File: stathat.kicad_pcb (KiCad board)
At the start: 4 copper layers, 65 x 56.5 mm, 40 parts, among them J1 Raspberry_Pi_2_3, J27 Conn_01x01, J28 Conn_01x01, J29 Conn_01x01, J31 Conn_01x01, J32 Conn_01x01, U26 HCPL3700, U27 HCPL3700, U28 HCPL3700

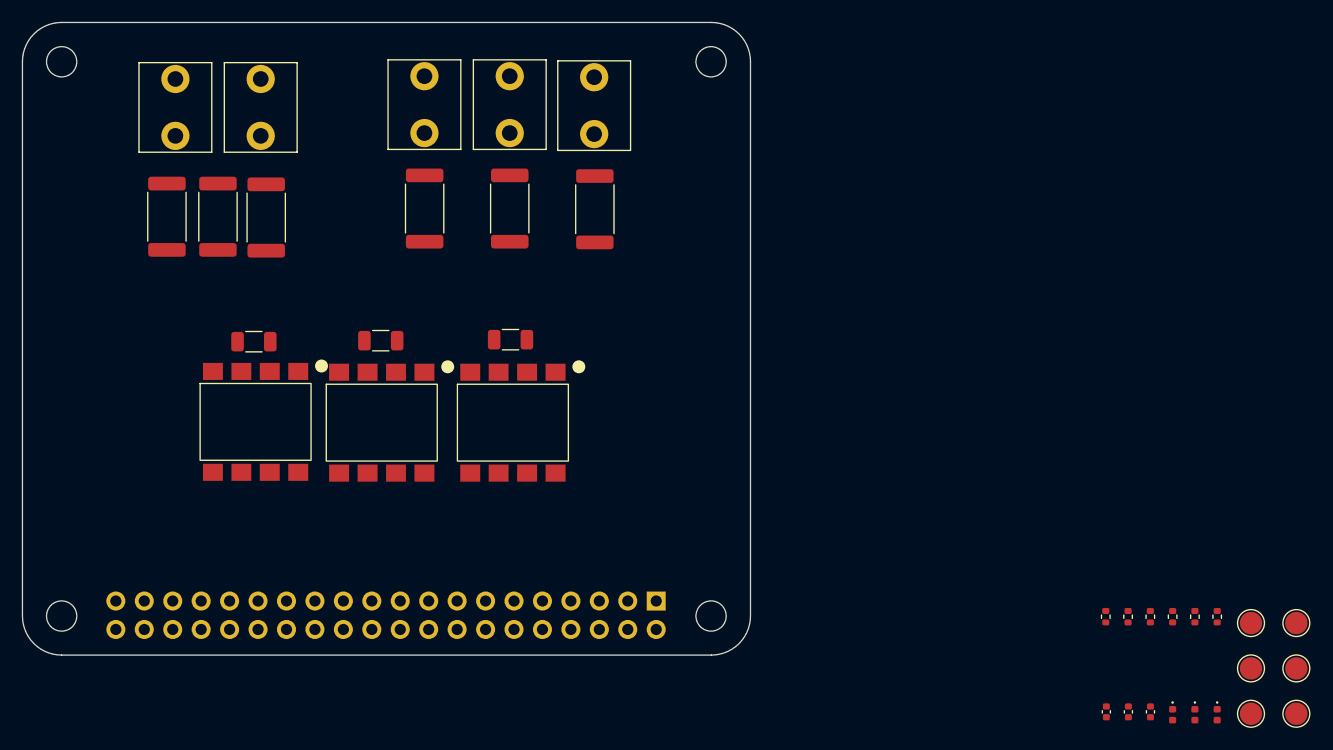
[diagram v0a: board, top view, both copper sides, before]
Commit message: fixed schematic. added part numbers. routed PCB
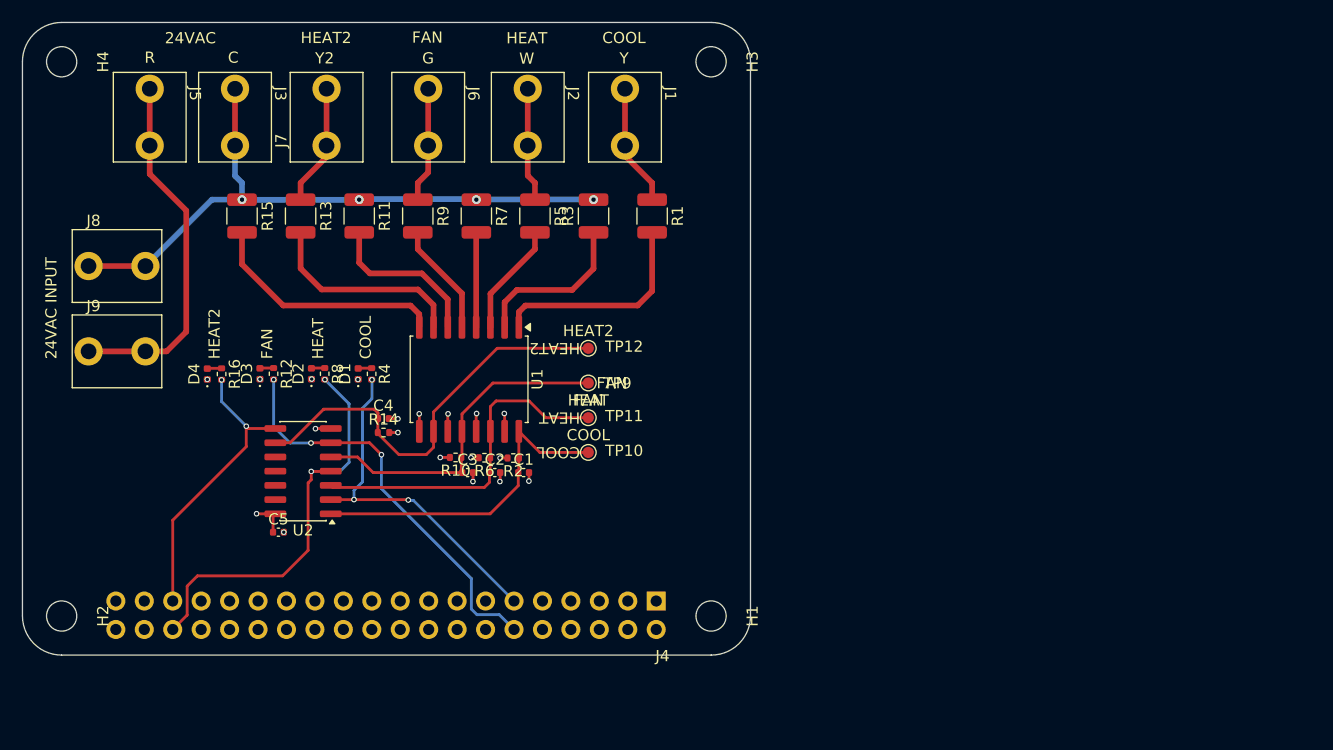
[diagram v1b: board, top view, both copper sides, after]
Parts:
- removed C31, C32, C47: 10uF, Resistor_SMD:R_1206_3216Metric
- removed R52, R62: 261, Resistor_SMD:R_0402_1005Metric
- removed TP42, TP43, TP46, TP47, TP48, TP51: TestPoint, TestPoint:TestPoint_Pad_D2.0mm
- removed U26, U28: HCPL3700, stathat:HCPL3700SV
- added C4: 2.2uF, Capacitor_SMD:C_0402_1005Metric, F.Cu at (139.4, 104.7)
- added C5: 0.1uF, Capacitor_SMD:C_0402_1005Metric, F.Cu at (130.0, 114.8)
- added D4: GREEN_LED, LED_SMD:LED_0402_1005Metric, F.Cu at (123.7, 100.7)
- added J7: Conn_01x01, stathat:63862-1, F.Cu at (134.3, 77.8)
- added J8: Conn_01x01, stathat:63862-1, F.Cu at (115.6, 91.1)
- added J9: Conn_01x01, stathat:63862-1, F.Cu at (115.6, 98.7)
- added R12: 2.2k, Resistor_SMD:R_0402_1005Metric, F.Cu at (129.6, 100.7)
- added R13: 5k, Resistor_SMD:R_1210_3225Metric, F.Cu at (132.0, 86.6)
- added R14: 10k, Resistor_SMD:R_0402_1005Metric, F.Cu at (139.4, 105.9)
- added R15: 5k, Resistor_SMD:R_1210_3225Metric, F.Cu at (126.8, 86.6)
- added R16: 2.2k, Resistor_SMD:R_0402_1005Metric, F.Cu at (124.9, 100.7)
- added R4: 2.2k, Resistor_SMD:R_0402_1005Metric, F.Cu at (138.3, 100.7)
- added TP10: COOL, stathat:TestPoint_Pad_D1.0mm, F.Cu at (157.7, 107.7)
- added TP11: HEAT, stathat:TestPoint_Pad_D1.0mm, F.Cu at (157.7, 104.6)
- added TP12: HEAT2, stathat:TestPoint_Pad_D1.0mm, F.Cu at (157.7, 98.4)
- added TP9: FAN, stathat:TestPoint_Pad_D1.0mm, F.Cu at (157.7, 101.5)
- added U2: 74HC14, Package_SO:SOIC-14_3.9x8.7mm_P1.27mm, F.Cu at (132.2, 109.4)
- C1: renamed from C44; value 0.1uF -> 2.2uF
- C2: renamed from C45; value 0.1uF -> 2.2uF
- C3: renamed from C49; value 0.1uF -> 2.2uF
- R1: renamed from R58; value 2k/3W -> 5k; footprint Resistor_SMD:R_2512_6332Metric -> Resistor_SMD:R_1210_3225Metric
- R10: renamed from R63; value 10K -> 10k
- R11: renamed from R65; value 2k/3W -> 5k; footprint Resistor_SMD:R_2512_6332Metric -> Resistor_SMD:R_1210_3225Metric
- R2: renamed from R54; value 10K -> 10k
- R3: renamed from R59; value 2k/3W -> 5k; footprint Resistor_SMD:R_2512_6332Metric -> Resistor_SMD:R_1210_3225Metric
- R5: renamed from R60; value 2k/3W -> 5k; footprint Resistor_SMD:R_2512_6332Metric -> Resistor_SMD:R_1210_3225Metric
- R6: renamed from R55; value 10K -> 10k
- R7: renamed from R61; value 2k/3W -> 5k; footprint Resistor_SMD:R_2512_6332Metric -> Resistor_SMD:R_1210_3225Metric
- R8: renamed from R53; value 261 -> 2.2k
- R9: renamed from R64; value 2k/3W -> 5k; footprint Resistor_SMD:R_2512_6332Metric -> Resistor_SMD:R_1210_3225Metric
- U1: renamed from U27; value HCPL3700 -> LTV-844S; footprint stathat:HCPL3700SV -> Package_SO:SOIC-16W_7.5x10.3mm_P1.27mm
- moved D3 87.0 mm to (128.3, 100.7), turned to 90 degrees
- moved D2 84.6 mm to (132.9, 100.7), turned to 90 degrees
- moved D1 82.5 mm to (137.1, 100.7), turned to 90 degrees
- moved R8 80.7 mm to (134.1, 100.7)
- moved R6 61.1 mm to (148.4, 108.2), turned to 180 degrees
- moved C3 60.9 mm to (146.9, 109.5), turned to 0 degrees
- moved R2 60.6 mm to (151.0, 108.2), turned to 180 degrees
- moved C2 60.5 mm to (149.3, 109.5), turned to 0 degrees
- moved C1 59.9 mm to (151.9, 109.5), turned to 0 degrees
- moved R10 59.8 mm to (145.8, 108.2), turned to 180 degrees
- moved R3 33.5 mm to (158.1, 86.6)
- moved R7 27.6 mm to (147.7, 86.6)
- moved U1 19.4 mm to (147.0, 101.2), turned to -90 degrees
- moved R9 15.8 mm to (142.4, 86.6)
- moved J6 14.9 mm to (143.4, 77.8)
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- renumbered D28 to D1, D29 to D2, D31 to D3, J27 to J1, J28 to J2, J29 to J3, J1 to J4, J31 to J5, J32 to J6
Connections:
- net Net-(J27-Pin_1) renamed /COOL_24VAC
- net Net-(J28-Pin_1) renamed /HEAT_24VAC
- net Net-(J32-Pin_1) renamed /FAN_24VAC
- C1 pad 1: /+3.3V -> /THERM_COOL_RAW
- C1 pad 2: GND -> /GND
- C2 pad 1: /+3.3V -> /THERM_HEAT_RAW
- C2 pad 2: GND -> /GND
- C3 pad 1: /+3.3V -> /THERM_FAN_RAW
- C3 pad 2: GND -> /GND
- D1 pad 1: /THERM_COOL -> /GND
- D2 pad 1: /THERM_HEAT -> /GND
- D3 pad 1: /THERM_FAN -> /GND
- J4 pad 14: GND -> /GND
- J4 pad 2: /5V -> unconnected-(J4-5V-Pad2)
- J4 pad 20: GND -> /GND
- J4 pad 25: GND -> /GND
- J4 pad 30: GND -> /GND
- J4 pad 34: GND -> /GND
- J4 pad 35: unconnected-(J1-GPIO19/MISO1-Pad35) -> /THERM_HEAT2
- J4 pad 39: GND -> /GND
- J4 pad 4: /5V -> unconnected-(J4-5V-Pad4)
- J4 pad 6: GND -> /GND
- J4 pad 9: GND -> /GND
- R1 pad 2: Net-(R58-Pad2) -> Net-(U1A-A1)
- R10 pad 1: /THERM_FAN -> /THERM_FAN_RAW
- R10 pad 2: /+3.3V -> /3V3
- R11 pad 2: Net-(R65-Pad2) -> Net-(U1C-A2)
- R2 pad 1: /THERM_COOL -> /THERM_COOL_RAW
- R2 pad 2: /+3.3V -> /3V3
- R3 pad 1: Net-(R59-Pad1) -> Net-(U1A-A2)
- R5 pad 2: Net-(R60-Pad2) -> Net-(U1B-A1)
- R6 pad 1: /THERM_HEAT -> /THERM_HEAT_RAW
- R6 pad 2: /+3.3V -> /3V3
- R8 pad 2: /+3.3V -> /THERM_HEAT
- R9 pad 2: Net-(R64-Pad2) -> Net-(U1C-A1)
- U1 pad 1: Net-(R60-Pad2) -> Net-(U1A-A1)
- U1 pad 2: Net-(U27-DC+) -> Net-(U1A-A2)
- U1 pad 3: Net-(U27-DC-) -> Net-(U1B-A1)
- U1 pad 5: GND -> Net-(U1C-A1)
- U1 pad 6: /THERM_HEAT -> Net-(U1C-A2)
- U1 pad 7: (no net) -> Net-(U1D-A1)
- U1 pad 8: /+3.3V -> Net-(U1D-A2)
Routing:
- net /-24VAC: track 0.00 -> 57.8 mm, vias 0 -> 4
- net /THERM_HEAT2_RAW: track 0.00 -> 37.8 mm
- net /THERM_HEAT: track 0.00 -> 37.5 mm, vias 0 -> 2
- net /THERM_FAN: track 0.00 -> 36.6 mm, vias 0 -> 3
- net /+24VAC: track 0.00 -> 32.5 mm
- net /THERM_COOL: track 0.00 -> 31.5 mm, vias 0 -> 3
- net /THERM_HEAT_RAW: track 0.00 -> 30.7 mm
- net /THERM_FAN_RAW: track 0.00 -> 30.1 mm
- net /THERM_COOL_RAW: track 0.00 -> 29.5 mm
- net /THERM_HEAT2: track 0.00 -> 26.1 mm, vias 0 -> 2
- net Net-(U1D-A2): track 0.00 -> 21.7 mm
- net Net-(U1A-A1): track 0.00 -> 19.3 mm
- net Net-(U1D-A1): track 0.00 -> 18.4 mm
- net Net-(U1A-A2): track 0.00 -> 14.7 mm
- net Net-(U1C-A2): track 0.00 -> 14.5 mm
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- added copper zone on In2.Cu, net /3V3
- added copper zone on In1.Cu, net /GND
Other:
- board text added: "24VAC"
- board text added: "24VAC INPUT"
- board text added: "C"
- board text added: "COOL"
- board text added: "FAN"
- board text added: "G"
- board text added: "HEAT"
- board text added: "HEAT2"
- board text added: "R"
- board text added: "W"
- board text added: "Y"
- board text added: "Y2"

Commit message: added render, updated readme
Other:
- board text added: "StatHat v1"
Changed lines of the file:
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@@
 			(at 0 -1.17 90)
 			(layer "F.SilkS")
+			(hide yes)
 			(effects
 				(font
@@
 			(at 0 -1.16 0)
 			(layer "F.SilkS")
+			(hide yes)
 			(effects
 				(font
@@
 			(at 0 -3.7 90)
 			(layer "F.SilkS")
+			(hide yes)
 			(effects
 				(font
@@
 			(at 0 -1.17 90)
 			(layer "F.SilkS")
+			(hide yes)
 			(effects
 				(font
@@
 			(unlocked yes)
 			(layer "F.SilkS")
+			(hide yes)
 			(effects
 				(font
@@
 			(at -3.203 0.153 0)
 			(layer "F.SilkS")
+			(hide yes)
 			(effects
 				(font
@@
 		)
 		(property "Value" "HEAT"
-			(at 0 1.55 0)
+			(at -7.975 -1.75 0)
 			(layer "F.SilkS")
+			(hide yes)
 			(effects
 				(font
@@
 		)
 		(fp_text user "${VALUE}"
-			(at 0.729 0.591 180)
+			(at -1.075 -0.45 0)
 			(unlocked yes)
 			(layer "F.SilkS")
@@
 			(at 0 -1.16 0)
 			(layer "F.SilkS")
+			(hide yes)
 			(effects
 				(font
@@
 			(at 0 -1.17 0)
 			(layer "F.SilkS")
+			(hide yes)
 			(effects
 				(font
@@
 			(at 0 -1.16 0)
 			(layer "F.SilkS")
+			(hide yes)
 			(effects
 				(font
@@
 			(at 2.6 0.025 0)
 			(layer "F.SilkS")
+			(hide yes)
 			(effects
 				(font
@@
 		)
 		(property "Value" "FAN"
-			(at 0 1.55 0)
-			(layer "F.SilkS")
+			(at 7.675 1.025 0)
+			(layer "F.Fab")
 			(effects
 				(font
@@
 		)
 		(fp_text user "${VALUE}"
-			(at 0.729 0.591 0)
+			(at 1.075 0.575 0)
 			(unlocked yes)
 			(layer "F.SilkS")
@@
 			(at 0 -1.17 90)
 			(layer "F.SilkS")
+			(hide yes)
 			(effects
 				(font
@@
 			(unlocked yes)
 			(layer "F.SilkS")
+			(hide yes)
 			(effects
 				(font
@@
 			(at 0 -2.28 270)
 			(layer "F.SilkS")
+			(hide yes)
 			(effects
 				(font
@@
 			(at 0 -2.28 270)
 			(layer "F.SilkS")
+			(hide yes)
 			(effects
 				(font
@@
 			(unlocked yes)
 			(layer "F.SilkS")
+			(hide yes)
 			(effects
 				(font
@@
 			(at 0 -3.7 90)
 			(layer "F.SilkS")
+			(hide yes)
 			(effects
 				(font
@@
 			(at 0 -5.28 0)
 			(layer "F.SilkS")
+			(hide yes)
 			(effects
 				(font
@@
 			(at 4.91132 -0.55868 0)
 			(layer "F.SilkS")
+			(hide yes)
 			(effects
 				(font
@@
 			(pinfunction "GND_6")
 			(pintype "power_in")
+			(thermal_bridge_angle 45)
 		)
 		(pad "7" thru_hole oval
@@
 			(pinfunction "GND_9")
 			(pintype "power_in")
+			(thermal_bridge_angle 45)
 		)
 		(pad "10" thru_hole oval
@@
 			(pinfunction "GND_14")
 			(pintype "power_in")
+			(thermal_bridge_angle 45)
 		)
 		(pad "15" thru_hole oval
@@
 			(pinfunction "3V3_17")
 			(pintype "power_out")
+			(thermal_bridge_angle 45)
 		)
 		(pad "18" thru_hole oval
@@
 			(pinfunction "GND_20")
 			(pintype "power_in")
+			(thermal_bridge_angle 45)
 		)
 		(pad "21" thru_hole oval
@@
 			(pinfunction "GND_25")
 			(pintype "power_in")
+			(thermal_bridge_angle 45)
 		)
 		(pad "26" thru_hole oval
@@
 			(pinfunction "GND_30")
 			(pintype "power_in")
+			(thermal_bridge_angle 45)
 		)
 		(pad "31" thru_hole oval
@@
 			(pinfunction "GND_34")
 			(pintype "power_in")
+			(thermal_bridge_angle 45)
 		)
 		(pad "35" thru_hole oval
@@
 			(at 0 -2.28 270)
 			(layer "F.SilkS")
+			(hide yes)
 			(effects
 				(font
@@
 			(at 0 -2.28 270)
 			(layer "F.SilkS")
+			(hide yes)
 			(effects
 				(font
@@
 			(at 0 -1.17 90)
 			(layer "F.SilkS")
+			(hide yes)
 			(effects
 				(font
@@
 			(unlocked yes)
 			(layer "F.SilkS")
+			(hide yes)
 			(effects
 				(font
@@
 			(at 0 -1.17 0)
 			(layer "F.SilkS")
+			(hide yes)
 			(effects
 				(font
@@
 			(at 0 -1.16 0)
 			(layer "F.SilkS")
+			(hide yes)
 			(effects
 				(font
@@
 			(at 0 -1.17 90)
 			(layer "F.SilkS")
+			(hide yes)
 			(effects
 				(font
@@
 			(at 0 -2.28 90)
 			(layer "F.SilkS")
+			(hide yes)
 			(effects
 				(font
@@
 			(at 0 -1.16 0)
 			(layer "F.SilkS")
+			(hide yes)
 			(effects
 				(font
@@
 			(at 0 -1.17 90)
 			(layer "F.SilkS")
+			(hide yes)
 			(effects
 				(font
@@
 			(at -3.203 0.153 0)
 			(layer "F.SilkS")
+			(hide yes)
 			(effects
 				(font
@@
 			(at 0 1.55 0)
 			(layer "F.SilkS")
+			(hide yes)
 			(effects
 				(font
@@
 		)
 		(fp_text user "${VALUE}"
-			(at 0.729 0.591 180)
+			(at -1.075 -0.6 0)
 			(unlocked yes)
 			(layer "F.SilkS")
@@
 			(at -3.203 0.153 0)
 			(layer "F.SilkS")
+			(hide yes)
 			(effects
 				(font
@@
 			(at 0 1.55 0)
 			(layer "F.SilkS")
+			(hide yes)
 			(effects
 				(font
@@
 		)
 		(fp_text user "${VALUE}"
-			(at 0.729 0.591 180)
+			(at -1.075 -0.525 0)
 			(unlocked yes)
 			(layer "F.SilkS")
@@
 			(at 0 -1.17 0)
 			(layer "F.SilkS")
+			(hide yes)
 			(effects
 				(font
@@
 			(at 0 -6.1 90)
 			(layer "F.SilkS")
+			(hide yes)
 			(effects
 				(font
@@
 			(unlocked yes)
 			(layer "F.SilkS")
+			(hide yes)
 			(effects
 				(font
@@
 			(at 0 -2.28 270)
 			(layer "F.SilkS")
+			(hide yes)
 			(effects
 				(font
@@
 			(unlocked yes)
 			(layer "F.SilkS")
+			(hide yes)
 			(effects
 				(font
@@
 			(unlocked yes)
 			(layer "F.SilkS")
+			(hide yes)
 			(effects
 				(font
@@
 			(at 0 -1.17 0)
 			(layer "F.SilkS")
+			(hide yes)
 			(effects
 				(font
@@
 			(at 0 -2.28 270)
 			(layer "F.SilkS")
+			(hide yes)
 			(effects
 				(font
@@
 			(at 0 -3.7 90)
 			(layer "F.SilkS")
+			(hide yes)
 			(effects
 				(font
@@
 			(unlocked yes)
 			(layer "F.SilkS")
+			(hide yes)
 			(effects
 				(font
@@
 			(at 0 -2.28 270)
 			(layer "F.SilkS")
+			(hide yes)
 			(effects
 				(font
@@
 			(at 0 -1.17 90)
 			(layer "F.SilkS")
+			(hide yes)
 			(effects
 				(font
@@
 			(at 0 -3.7 90)
 			(layer "F.SilkS")
+			(hide yes)
 			(effects
 				(font
@@
 			(at 0 -1.17 90)
 			(layer "F.SilkS")
+			(hide yes)
 			(effects
 				(font
@@
 		)
 	)
+	(gr_text "StatHat v1"
+		(at 109.3 118.3 0)
+		(layer "F.SilkS")
+		(effects
+			(font
+				(size 2 2)
+				(thickness 0.3)
+			)
+			(justify left bottom)
+		)
+	)
 	(segment
 		(start 132.975 100.165)
@@
 		(polygon
 			(pts
-				(xy 104.677124 118.444869) (xy 123.700219 99.338744) (xy 174.101747 99.214165) (xy 174.15 128.95)
-				(xy 104.7 128.95)
+				(xy 106.214332 116.900951) (xy 123.700219 99.338744) (xy 172.77589 99.217442) (xy 172.820488 126.7)
+				(xy 106.23567 126.7)
+			)
+		)
+	)
+	(zone
+		(layers "In1.Cu" "In2.Cu")
+		(hatch edge 0.5)
+		(connect_pads
+			(clearance 0)
+		)
+		(min_thickness 0.25)
+		(keepout
+			(tracks allowed)
+			(vias allowed)
+			(pads allowed)
+			(copperpour not_allowed)
+			(footprints allowed)
+		)
+		(placement
+			(enabled no)
+			(sheetname "/")
+		)
+		(fill
+			(thermal_gap 0.5)
+			(thermal_bridge_width 0.5)
+			(island_removal_mode 0)
+		)
+		(polygon
+			(pts
+				(xy 115.375 120.875) (xy 163.85 120.975) (xy 163.85 123.51132) (xy 115.375 123.51132)
 			)
 		)
@@
 		(polygon
 			(pts
-				(xy 104.700377 118.505704) (xy 123.723472 99.399579) (xy 174.125 99.275) (xy 174.173253 129.010835)
-				(xy 104.723253 129.010835)
+				(xy 106.364404 116.834414) (xy 123.723472 99.399579) (xy 172.777855 99.27833) (xy 172.822109 126.55)
+				(xy 106.385562 126.55)
 			)
 		)
